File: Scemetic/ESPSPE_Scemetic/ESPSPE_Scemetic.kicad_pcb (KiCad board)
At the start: 2 copper layers, 76.3 x 31 mm, 53 parts, among them J1 Screw_Terminal_01x02, J2 Conn_01x01_Pin, SW1 RESET, T1 749070010, U1 DEVKIT_V1_ESP32-WROOM-32, U2 ADIN1110, U3 TVS_Diode_8240136, Y2 CFPX-180_830105863709

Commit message: Vias eingefügt
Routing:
- net GND: track 4.13 -> 70.0 mm, vias 0 -> 8
- net AVDD_H: track 182.3 -> 181.7 mm
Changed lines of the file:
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@@
+	)
+	(segment
+		(start 148.53 51.9925)
+		(end 148.5 51.9625)
+		(width 0.2)
+		(layer "F.Cu")
+		(net 1)
+	)
+	(segment
+		(start 150.9875 51.51)
+		(end 150.505 51.9925)
+		(width 0.2)
+		(layer "F.Cu")
+		(net 1)
+	)
+	(segment
+		(start 150.7 61.47)
+		(end 150.73 61.47)
+		(width 0.2)
+		(layer "F.Cu")
+		(net 1)
 	)
 	(segment
@@
 	)
 	(segment
-		(start 148.53 51.9925)
-		(end 148.5 51.9625)
-		(width 0.2)
-		(layer "F.Cu")
-		(net 1)
-	)
-	(segment
-		(start 150.9875 51.51)
-		(end 150.505 51.9925)
+		(start 150.93 61.47)
+		(end 151.9 60.5)
+		(width 0.2)
+		(layer "F.Cu")
+		(net 1)
+	)
+	(segment
+		(start 150.73 61.47)
+		(end 150.93 61.47)
+		(width 0.2)
+		(layer "F.Cu")
+		(net 1)
+	)
+	(segment
+		(start 150.87 61.47)
+		(end 152 62.6)
 		(width 0.2)
 		(layer "F.Cu")
@@
 	)
 	(segment
+		(start 150.73 61.47)
+		(end 149.7 62.5)
+		(width 0.2)
+		(layer "F.Cu")
+		(net 1)
+	)
+	(segment
 		(start 154.1 68.4)
 		(end 154.1 68.5375)
@@
 	)
 	(segment
+		(start 150.73 61.47)
+		(end 150.87 61.47)
+		(width 0.2)
+		(layer "F.Cu")
+		(net 1)
+	)
+	(via
+		(at 160.5 54)
+		(size 0.6)
+		(drill 0.3)
+		(layers "F.Cu" "B.Cu")
+		(net 1)
+	)
+	(via
+		(at 138.9 60.1)
+		(size 0.6)
+		(drill 0.3)
+		(layers "F.Cu" "B.Cu")
+		(net 1)
+	)
+	(via
+		(at 149.7 62.5)
+		(size 0.6)
+		(drill 0.3)
+		(layers "F.Cu" "B.Cu")
+		(net 1)
+	)
+	(via
+		(at 149.8 60.4)
+		(size 0.6)
+		(drill 0.3)
+		(layers "F.Cu" "B.Cu")
+		(net 1)
+	)
+	(via
+		(at 152 62.6)
+		(size 0.6)
+		(drill 0.3)
+		(layers "F.Cu" "B.Cu")
+		(net 1)
+	)
+	(via
+		(at 155.3 70.8)
+		(size 0.6)
+		(drill 0.3)
+		(layers "F.Cu" "B.Cu")
+		(net 1)
+	)
+	(via
+		(at 136.6 69.8)
+		(size 0.6)
+		(drill 0.3)
+		(layers "F.Cu" "B.Cu")
+		(net 1)
+	)
+	(via
+		(at 151.9 60.5)
+		(size 0.6)
+		(drill 0.3)
+		(layers "F.Cu" "B.Cu")
+		(net 1)
+	)
+	(segment
+		(start 153.1 48.4)
+		(end 157.2 48.4)
+		(width 0.2)
+		(layer "B.Cu")
+		(net 1)
+	)
+	(segment
+		(start 149.8 60.4)
+		(end 149 61.2)
+		(width 0.2)
+		(layer "B.Cu")
+		(net 1)
+	)
+	(segment
+		(start 140 61.2)
+		(end 138.9 60.1)
+		(width 0.2)
+		(layer "B.Cu")
+		(net 1)
+	)
+	(segment
+		(start 152 67.5)
+		(end 155.3 70.8)
+		(width 0.2)
+		(layer "B.Cu")
+		(net 1)
+	)
+	(segment
+		(start 149.7 62.5)
+		(end 143.9 62.5)
+		(width 0.2)
+		(layer "B.Cu")
+		(net 1)
+	)
+	(segment
+		(start 152 62.6)
+		(end 152 67.5)
+		(width 0.2)
+		(layer "B.Cu")
+		(net 1)
+	)
+	(segment
+		(start 152.6 59.8)
+		(end 152.6 48.9)
+		(width 0.2)
+		(layer "B.Cu")
+		(net 1)
+	)
+	(segment
+		(start 152.6 48.9)
+		(end 153.1 48.4)
+		(width 0.2)
+		(layer "B.Cu")
+		(net 1)
+	)
+	(segment
+		(start 149 61.2)
+		(end 140 61.2)
+		(width 0.2)
+		(layer "B.Cu")
+		(net 1)
+	)
+	(segment
+		(start 157.7 48.9)
+		(end 157.7 51.2)
+		(width 0.2)
+		(layer "B.Cu")
+		(net 1)
+	)
+	(segment
+		(start 143.9 62.5)
+		(end 136.6 69.8)
+		(width 0.2)
+		(layer "B.Cu")
+		(net 1)
+	)
+	(segment
+		(start 157.7 51.2)
+		(end 160.5 54)
+		(width 0.2)
+		(layer "B.Cu")
+		(net 1)
+	)
+	(segment
+		(start 151.9 60.5)
+		(end 152.6 59.8)
+		(width 0.2)
+		(layer "B.Cu")
+		(net 1)
+	)
+	(segment
+		(start 157.2 48.4)
+		(end 157.7 48.9)
+		(width 0.2)
+		(layer "B.Cu")
+		(net 1)
+	)
+	(segment
 		(start 149.9625 71)
 		(end 149.9625 69.0375)
@@
 		(width 0.2)
 		(layer "F.Cu")
-		(net 8)
-	)
-	(segment
-		(start 150.505 54.0375)
-		(end 150.505 53.505)
-		(width 0.2)
-		(layer "F.Cu")

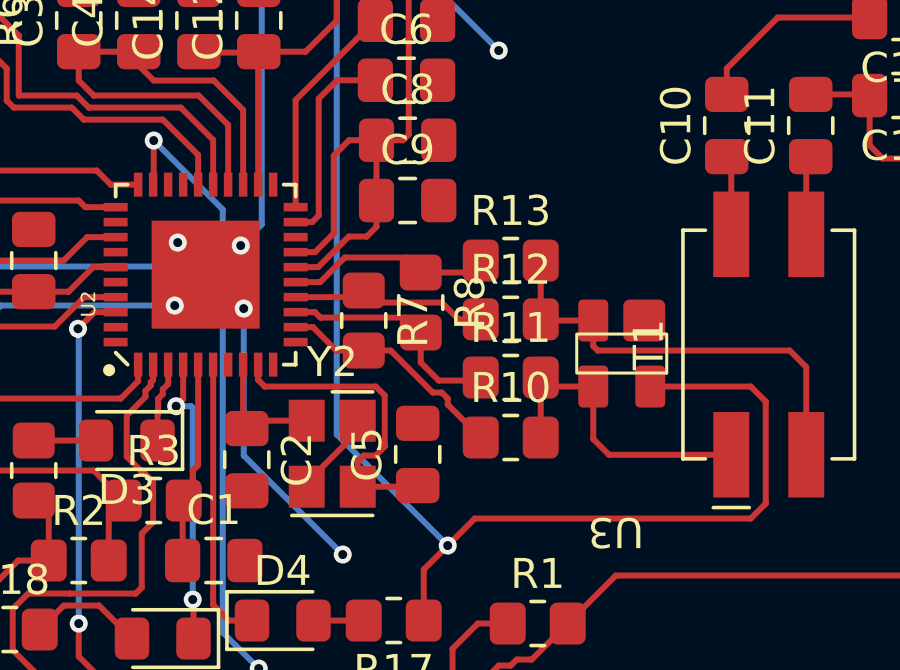
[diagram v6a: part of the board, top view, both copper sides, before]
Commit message: Bestellliste erstellt, Schaltplanänderung angepasst.
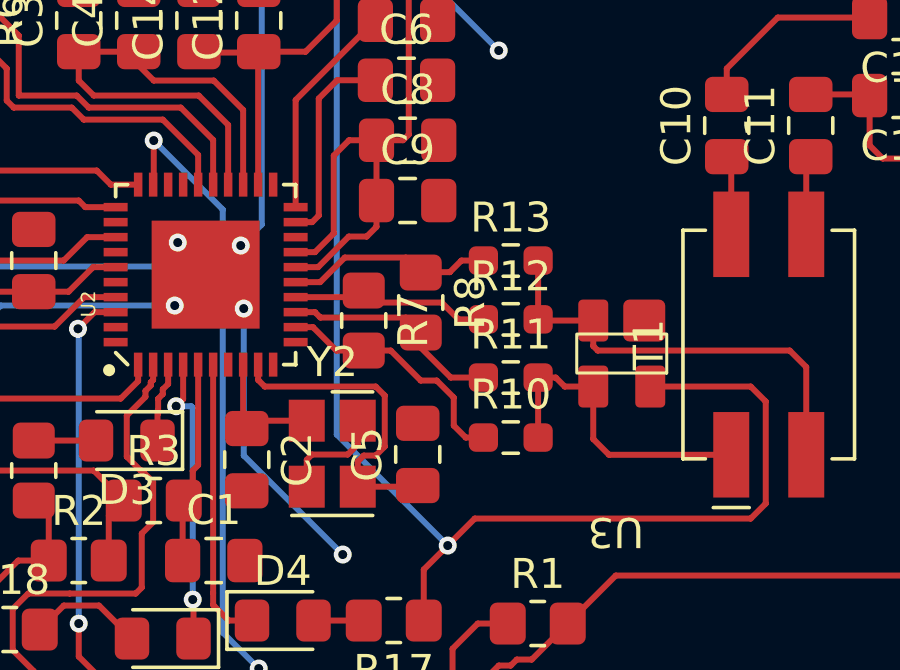
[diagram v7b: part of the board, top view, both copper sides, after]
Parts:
- R10, R13: footprint Resistor_SMD:R_0805_2012Metric_Pad1.20x1.40mm_HandSolder -> Resistor_SMD:R_0603_1608Metric_Pad0.98x0.95mm_HandSolder
- R11, R12: value 5.1k -> 4.99k; footprint Resistor_SMD:R_0805_2012Metric_Pad1.20x1.40mm_HandSolder -> Resistor_SMD:R_0603_1608Metric_Pad0.98x0.95mm_HandSolder
- R7, R8: value 10.2k -> 10k
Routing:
- net GND: track 70.0 -> 70.9 mm
